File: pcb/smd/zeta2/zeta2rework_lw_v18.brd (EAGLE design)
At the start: 80.3 x 45.7 mm, 94 parts, among them IC1 MAX6520, U5 DS18B20U+

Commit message: small changes
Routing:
- net +8V: track 246.2 -> 239.0 mm
- net GND: track 600.9 -> 602.2 mm
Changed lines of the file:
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@@
 <wire x1="44.9072" y1="39.8272" x2="44.7294" y2="40.005" width="0.254" layer="1"/>
 <wire x1="8.55" y1="34.5994" x2="8.55" y2="33.995" width="0.4064" layer="1"/>
-<wire x1="8.55" y1="33.995" x2="8.5725" y2="33.9725" width="0.4064" layer="1"/>
-<wire x1="8.5725" y1="33.9725" x2="8.89" y2="33.655" width="0.4064" layer="1"/>
+<wire x1="8.55" y1="33.995" x2="8.89" y2="33.655" width="0.4064" layer="1"/>
 <wire x1="8.89" y1="33.655" x2="9.2" y2="33.965" width="0.4064" layer="1"/>
 <wire x1="9.2" y1="33.965" x2="9.2" y2="34.5994" width="0.4064" layer="1"/>
-<wire x1="9.85" y1="31.9994" x2="9.85" y2="32.695" width="0.4064" layer="1"/>
-<wire x1="9.85" y1="32.695" x2="8.89" y2="33.655" width="0.4064" layer="1"/>
 <wire x1="56.515" y1="33.274" x2="56.515" y2="34.925" width="0.6096" layer="16"/>
 <via x="56.515" y="34.925" extent="1-16" drill="0.35"/>
@@
 <wire x1="54.003" y1="23.3426" x2="44.803" y2="23.3426" width="0.6096" layer="1"/>
 <wire x1="15.748" y1="10.541" x2="12.424" y2="10.541" width="2.54" layer="16"/>
-<wire x1="8.5725" y1="33.9725" x2="7.1737" y2="33.9725" width="0.508" layer="1"/>
 <wire x1="7.1737" y1="33.9725" x2="6.9206" y2="34.2256" width="0.508" layer="1"/>
 <wire x1="5.08" y1="19.79" x2="8.255" y2="16.615" width="1.27" layer="1"/>
@@
 <wire x1="54.003" y1="23.3426" x2="55.88" y2="23.3426" width="0.6096" layer="1"/>
 <wire x1="55.88" y1="23.3426" x2="55.88" y2="22.225" width="0.6096" layer="1"/>
+<wire x1="8.5598" y1="33.3248" x2="8.89" y2="33.655" width="0.4064" layer="1"/>
+<wire x1="6.985" y1="34.29" x2="7.9502" y2="33.3248" width="0.4064" layer="1"/>
+<wire x1="7.9502" y1="33.3248" x2="8.5598" y2="33.3248" width="0.4064" layer="1"/>
+<wire x1="9.85" y1="33.203" x2="9.7536" y2="33.2994" width="0.4064" layer="1"/>
+<wire x1="9.7536" y1="33.2994" x2="9.2456" y2="33.2994" width="0.4064" layer="1"/>
+<wire x1="9.2456" y1="33.2994" x2="8.89" y2="33.655" width="0.4064" layer="1"/>
+<wire x1="9.85" y1="31.9994" x2="9.85" y2="33.203" width="0.4064" layer="1"/>
 </signal>
 <signal name="V+">
@@
 <wire x1="56.9976" y1="10.5918" x2="59.0068" y2="10.5918" width="1.016" layer="1"/>
 <wire x1="59.0068" y1="10.5918" x2="59.0804" y2="10.6654" width="1.016" layer="1"/>
-<wire x1="7.815" y1="46.55" x2="12.309" y2="51.044" width="1.016" layer="16"/>
-<wire x1="7.815" y1="46.55" x2="6.985" y2="46.55" width="1.016" layer="16"/>
 <wire x1="15.748" y1="19.939" x2="21.717" y2="13.97" width="2.54" layer="16"/>
 <wire x1="21.717" y1="13.97" x2="39.37" y2="13.97" width="2.54" layer="16"/>
@@
 <wire x1="76.7875" y1="48.065" x2="73.855" y2="48.065" width="1.778" layer="16"/>
 <wire x1="73.855" y1="48.065" x2="71.13" y2="50.79" width="1.778" layer="16"/>
-<wire x1="11.225" y1="50.79" x2="6.985" y2="46.55" width="1.778" layer="16"/>
-<wire x1="71.13" y1="50.79" x2="11.225" y2="50.79" width="1.778" layer="16"/>
+<wire x1="11.225" y1="50.79" x2="71.13" y2="50.79" width="1.778" layer="16"/>
 <wire x1="6.985" y1="46.55" x2="3.8575" y2="46.55" width="1.778" layer="16"/>
 <wire x1="11.176" y1="19.939" x2="15.748" y2="19.939" width="1.778" layer="16"/>
@@
 <wire x1="2.735" y1="46.55" x2="1.905" y2="45.72" width="1.778" layer="16"/>
 <wire x1="1.905" y1="45.72" x2="1.905" y2="29.21" width="1.778" layer="16"/>
+<wire x1="6.985" y1="46.55" x2="11.225" y2="50.79" width="1.778" layer="16"/>
 </signal>
 <signal name="M_DIR_1">

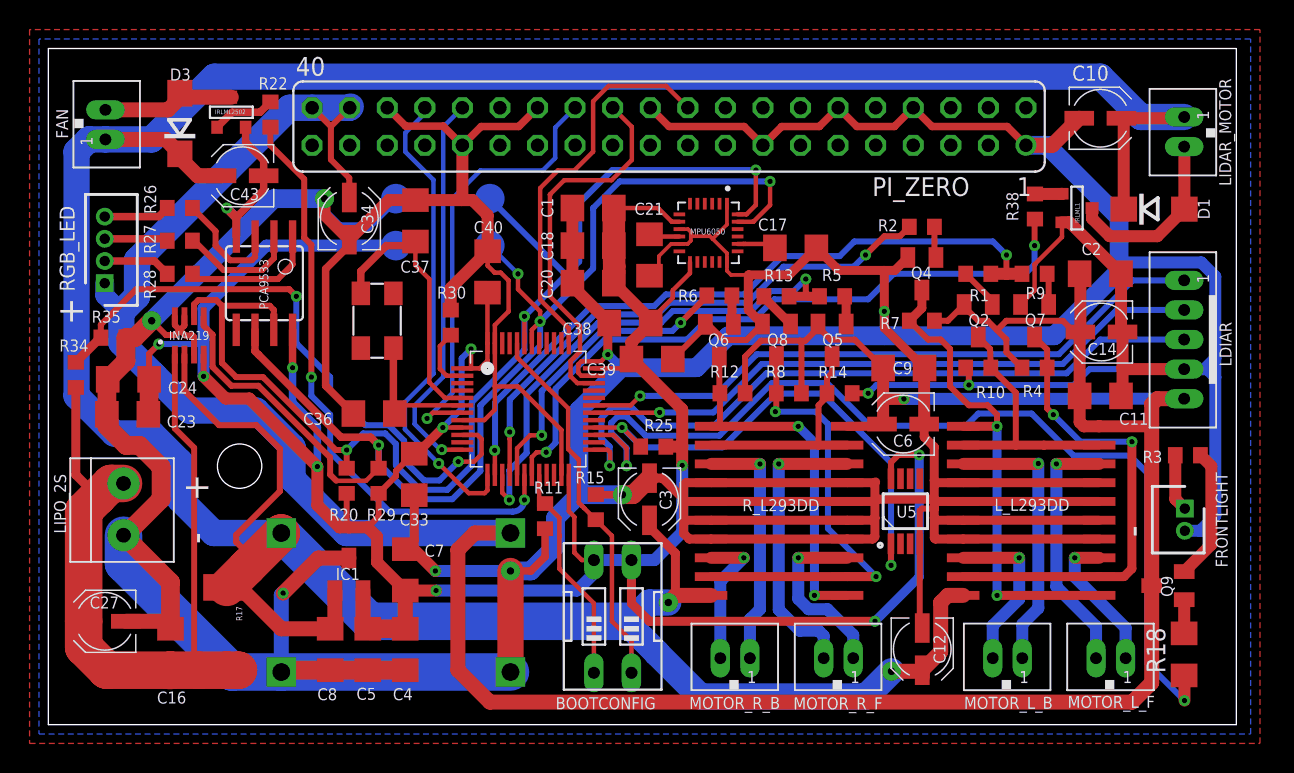
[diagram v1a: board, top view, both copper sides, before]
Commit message: using ph for leds again
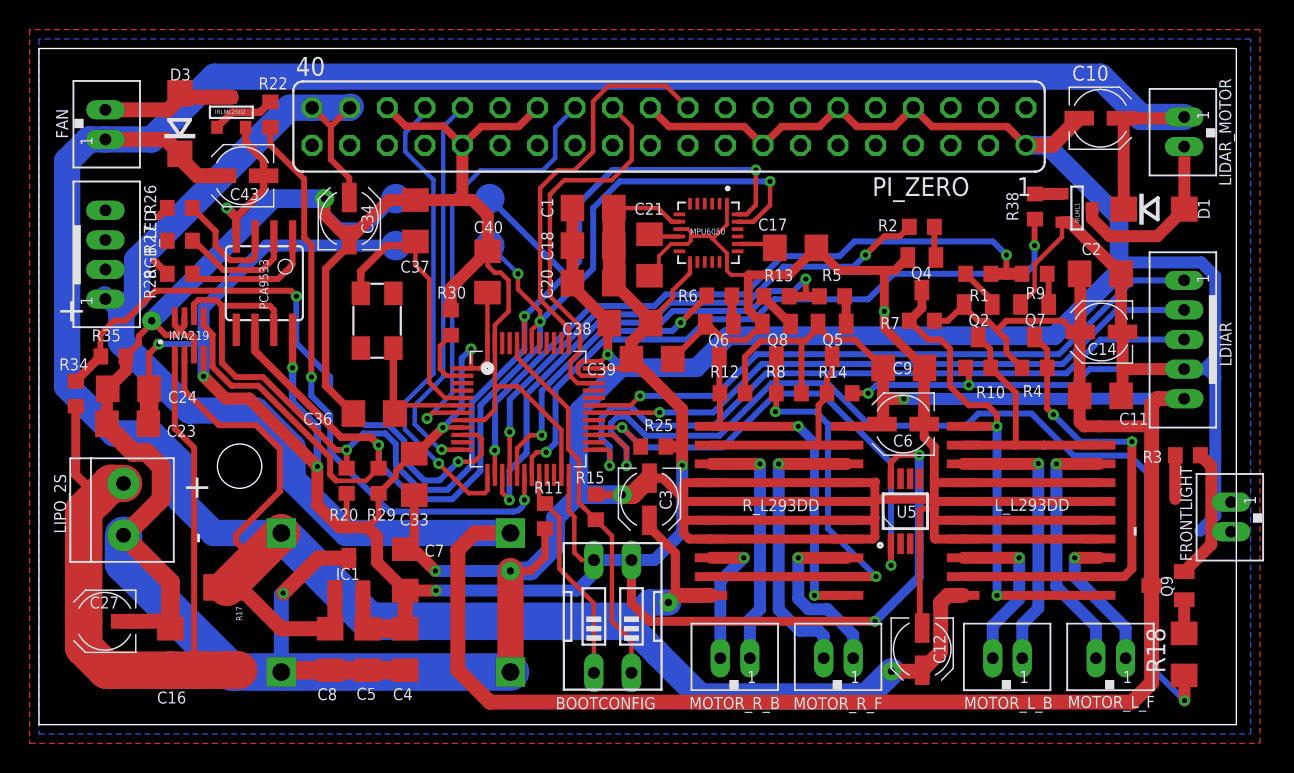
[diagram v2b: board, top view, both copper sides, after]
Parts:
- FRONTLIGHT: value B2B-ZR(LF)(SN) -> JST-PH_2-PIN_HEADER; device B2B-ZR(LF)(SN):SHDR2W50P0X150_1X2_450X350X450 -> srg:JST_B2B-PH_HEADER
- RGB_LED: value B4B-ZR(LF)(SN) -> JST-PH_4-PIN_HEADER; device B4B-ZR(LF)(SN):SHDR4W50P0X150_1X4_750X350X450 -> srg:JST_B4B-PH_HEADER
- moved FRONTLIGHT 3.24 mm to (80.0, 21.0)
- moved RGB_LED 1.91 mm to (3.81, 38.7)
- moved R34 1.27 mm to (1.85, 29.4)
- moved R35 1.27 mm to (4.39, 31.9)
- moved C24 0.64 mm to (5.41, 29.7)
- moved C23 0.63 mm to (5.36, 27.3)
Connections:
- net +5V: now also RGB_LED.P1; no longer RGB_LED.1
- net GND: now also FRONTLIGHT.P2; no longer FRONTLIGHT.2
- net N$28: now also FRONTLIGHT.P1; no longer FRONTLIGHT.1
- net N$31: now also RGB_LED.P4; no longer RGB_LED.4
- net N$33: now also RGB_LED.P3; no longer RGB_LED.3
- net N$35: now also RGB_LED.P2; no longer RGB_LED.2
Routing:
- net N$33: track 4.28 -> 0.18 mm
- net N$31: track 4.47 -> 0.82 mm
- net N$35: track 4.59 -> 1.22 mm
- net GND: track 602.2 -> 600.9 mm
- net V+: track 53.8 -> 52.6 mm
- net N$28: track 3.87 -> 2.96 mm
- net +5V: track 225.2 -> 224.4 mm
- net BAT_LVL: track 41.7 -> 42.5 mm
- net +3V3: track 199.8 -> 200.4 mm
- net +8V: track 239.0 -> 239.6 mm
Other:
- board size 80.3 x 45.7 mm -> 81 x 45.7 mm
